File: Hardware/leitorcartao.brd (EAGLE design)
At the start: 34.5 x 56.7 mm, 156 parts, among them IC1 TL084, IC2 TL084, Q1 DMN3404, Q4 BC847ALT1SMD, Q5 BC847ALT1SMD, Q6 BC847ALT1SMD, Q7 BC847ALT1SMD, Q8 MMBT4403, Q9 MMBT4401, U1 SAMD20E14A-AUT, U3 TLV1117-50CDCYR, U4 MFRC52202HN1, U5 LP2985-33DBVR, X1 ANTENA, X2 MIFARE ANTENA

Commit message: Mudanças no layout.
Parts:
- removed X2: MIFARE ANTENA, con-molex:22-23-2021
- added C13, C58: 0.1u, RFiD:C0402
- added X3: ANTENA, RFiD:22-23-2021
- added Y2: (no value), RFiD:HC49/S
- D1: value (none) -> BYG20J; device RFiD:DO214AA -> RFiD:SMA
- D3: value US1J-13-F -> BYG20J
- SWD: device pinhead:1X05 -> RFiD:1X05
- X1: value ANTENA -> MIFARE; device con-molex:22-23-2021 -> RFiD:22-23-2021
- moved R50 176.9 mm to (28.6, 48.1), turned to 90 degrees
- moved C19 142.3 mm to (43.9, 29.1)
- moved C24 142.3 mm to (43.9, 19.5)
- moved C29 142.3 mm to (43.9, 14.7)
- moved R16 142.3 mm to (43.9, 24.3)
- moved R20 142.3 mm to (43.9, 9.90)
- moved R49 142.3 mm to (43.9, 6.50)
- moved Q9 126.8 mm to (12.4, 44.2), flipped to the bottom
- moved Q8 120.0 mm to (12.4, 44.2), turned to 180 degrees
- moved C18 109.0 mm to (30.6, 41.3), flipped to the bottom, turned to 90 degrees
- moved C16 106.8 mm to (31.2, 43.1), flipped to the bottom
- moved Q1 106.7 mm to (12.4, 40.2)
- moved R9 101.7 mm to (32.4, 40.7), flipped to the bottom, turned to 180 degrees
- moved R7 98.8 mm to (32.4, 41.9), flipped to the bottom
- moved R4 96.8 mm to (33.0, 43.7), flipped to the bottom, turned to 270 degrees
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- renumbered QZ1 to Y1
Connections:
- new net XIN: C58.1, U1.15, Y2.1
- new net XOUT: C13.1, U1.16, Y2.2
- net +12V: now also D1.K; no longer D1.C
- net GND: now also C13.2, C58.2
- net N$11: now also X3.1; no longer X1.1
- net N$38: now also X1.1; no longer X2.2
- net N$39: now also X1.2; no longer X2.1
- net N$9: now also X3.2; no longer X1.2
- net USART-RX: no longer U1.15
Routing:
- net USART-RX: track 15.1 -> 0.00 mm
- net +5V: track 37.1 -> 22.4 mm
- net LED-INPUT: track 13.9 -> 1.75 mm
- net MIFARE-SDA: track 15.4 -> 9.24 mm, vias 1 -> 0
- net D0/TX/CLK: track 5.77 -> 0.00 mm
- net MIFARE-SCL: track 10.8 -> 5.27 mm, vias 3 -> 2
- net CARD-PRES: track 5.21 -> 0.00 mm
- net N$41: track 4.71 -> 0.00 mm
- net D1/DATA: track 4.34 -> 0.00 mm
- net +12V: track 80.4 -> 78.4 mm
- net BUZZER: track 2.11 -> 0.11 mm
- net GND: track 39.5 -> 41.3 mm, vias 34 -> 38
- net VCC/2: track 2.22 -> 0.37 mm
- net N$39: track 2.56 -> 0.73 mm
- net N$38: track 2.56 -> 0.73 mm
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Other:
- board text added: "1"
- board text added: "10"
- board text added: "15"
- board text added: "20"
- board text added: "5"

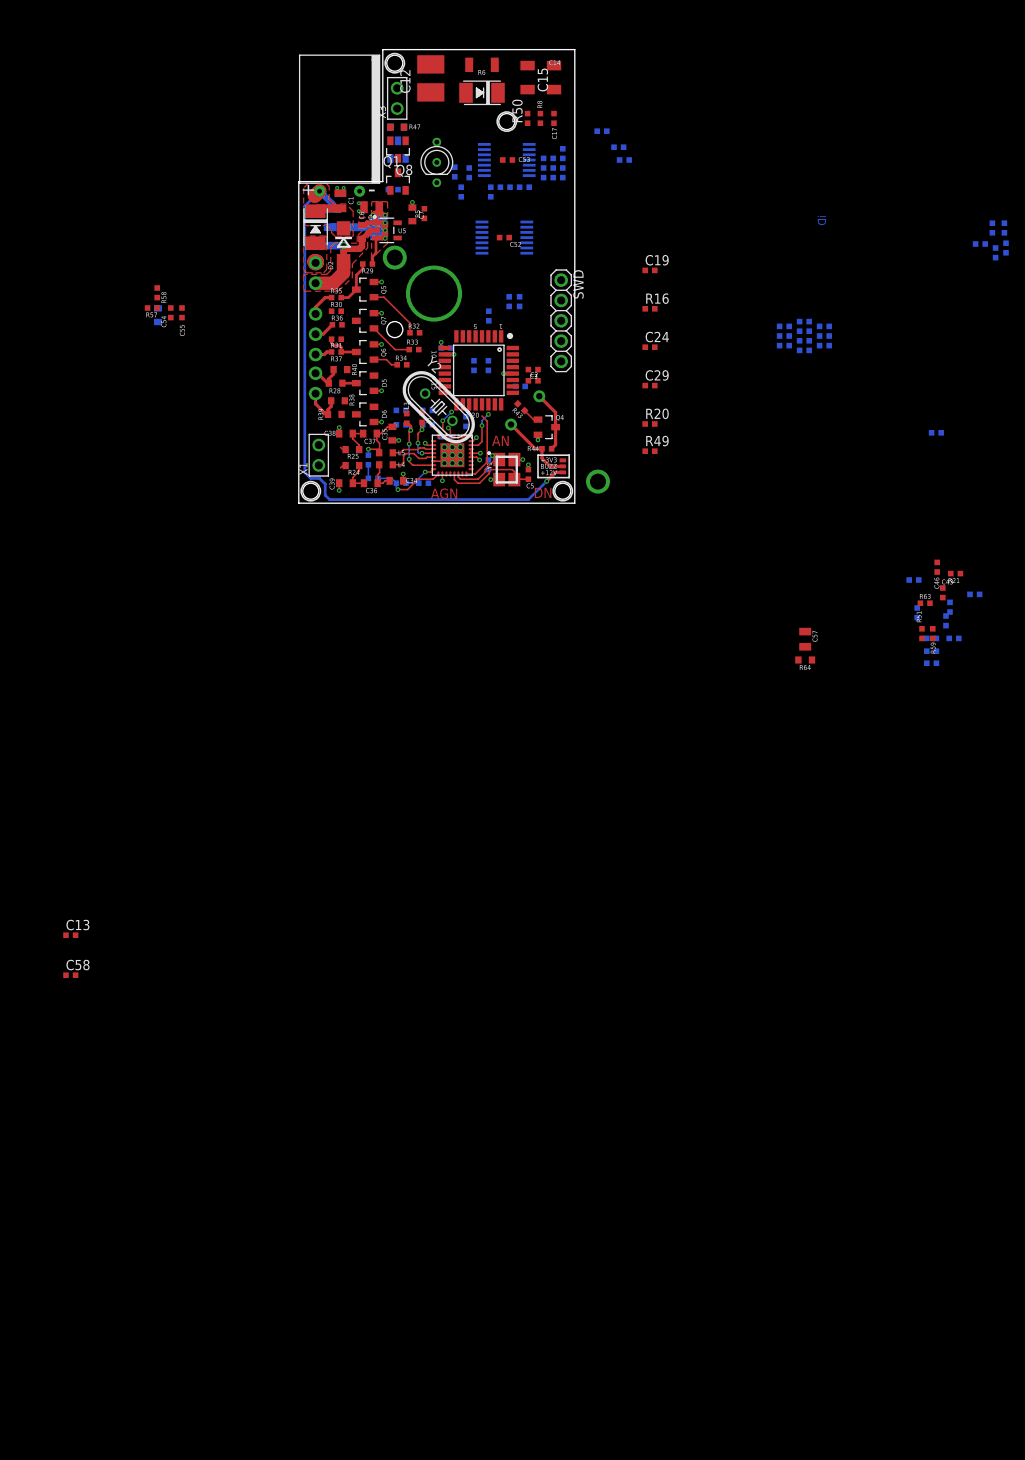
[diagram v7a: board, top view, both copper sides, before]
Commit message: Nova versão do roteamento. Tentativa de isolar tudo no top para DFM.
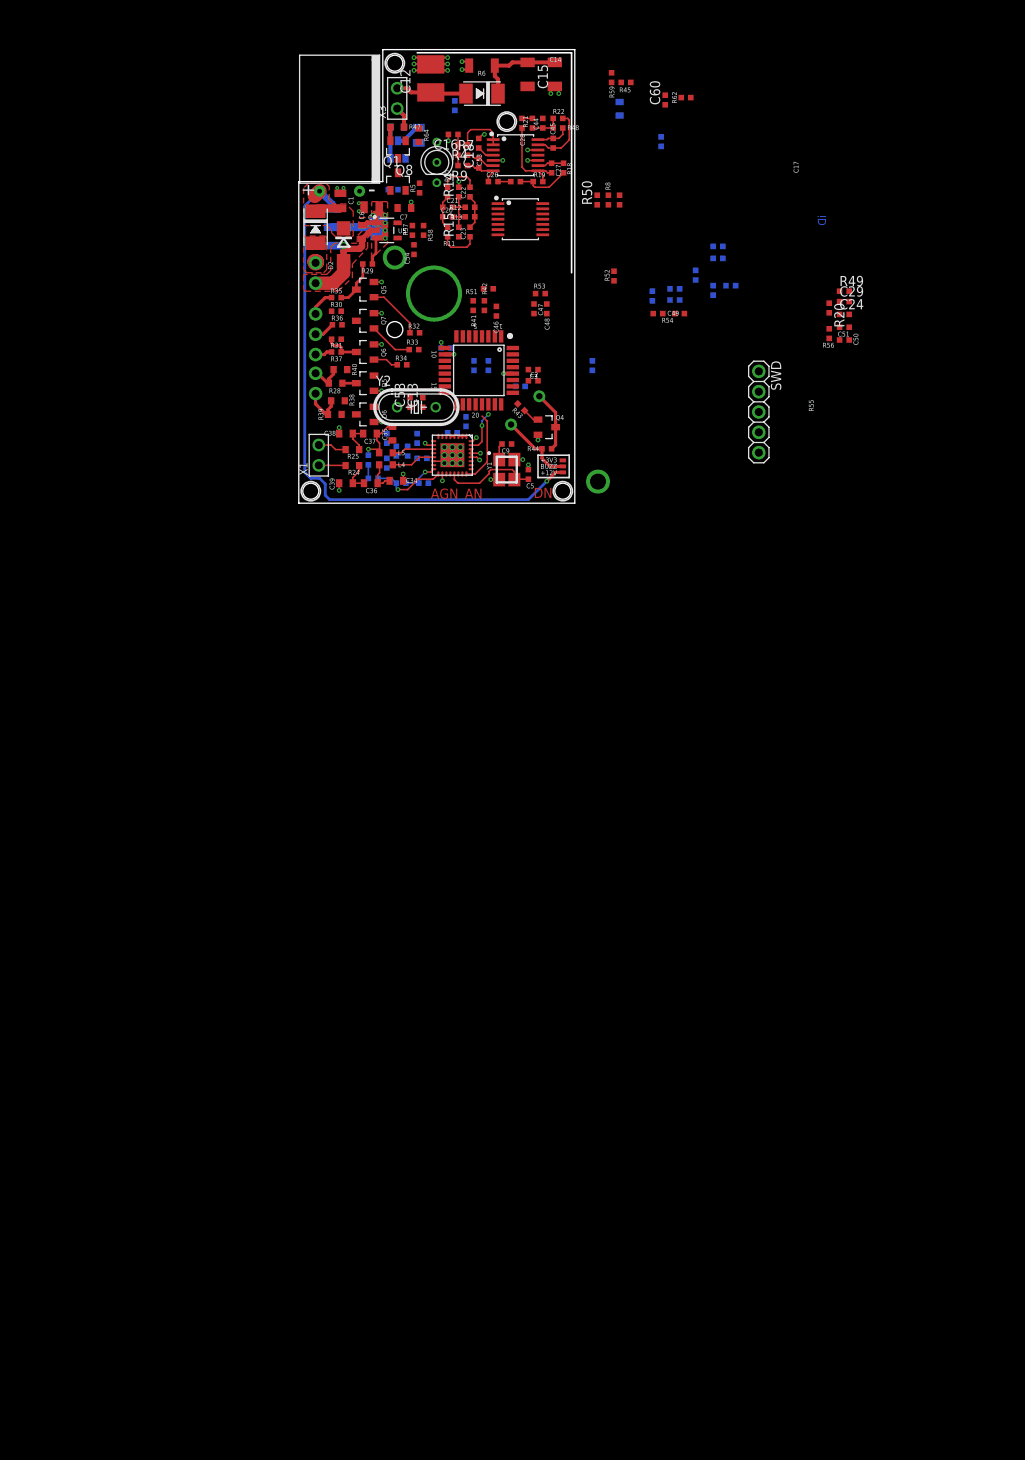
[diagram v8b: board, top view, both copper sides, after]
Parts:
- added C59, C60: 0.1u, RFiD:C0402
- moved C58 83.2 mm to (13.9, 12.6), turned to 90 degrees
- moved R64 81.5 mm to (15.0, 46.0), turned to 270 degrees
- moved R59 80.3 mm to (39.1, 53.2)
- moved C13 79.8 mm to (15.5, 12.6), turned to 90 degrees
- moved C57 79.4 mm to (15.0, 46.0), flipped to the bottom, turned to 270 degrees
- moved R21 77.3 mm to (29.2, 47.5), turned to 270 degrees
- moved C45 77.2 mm to (31.8, 45.0), flipped to the top, turned to 90 degrees
- moved C28 75.2 mm to (27.9, 47.5), flipped to the top, turned to 90 degrees
- moved R51 69.2 mm to (23.7, 26.8), turned to 0 degrees
- moved R53 67.3 mm to (30.2, 26.2), flipped to the top, turned to 0 degrees
- moved R42 65.7 mm to (23.2, 24.7), flipped to the top
- moved R41 65.6 mm to (21.8, 24.7), flipped to the top
- moved C47 64.6 mm to (29.4, 24.3), flipped to the top, turned to 270 degrees
- moved C48 64.4 mm to (31.0, 24.3), flipped to the top, turned to 270 degrees
- moved C46 63.7 mm to (24.7, 24.0)
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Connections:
- net GND: now also C59.2, C60.2
- net V+: now also C59.1, C60.1
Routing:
- net GND: track 41.3 -> 60.0 mm, vias 38 -> 48
- net N$13: track 0.00 -> 11.3 mm
- net N$56: track 0.00 -> 10.5 mm
- net ASK: track 0.00 -> 9.94 mm
- net N$4: track 9.71 -> 0.00 mm, vias 3 -> 0
- net N$9: track 0.00 -> 8.88 mm
- net N$64: track 0.00 -> 7.86 mm
- net N$17: track 0.00 -> 7.00 mm
- net N$22: track 0.00 -> 6.73 mm
- net N$2: track 6.56 -> 0.00 mm, vias 3 -> 0
- net N$10: track 0.00 -> 6.53 mm
- net N$5: track 8.20 -> 2.09 mm, vias 1 -> 0
- net N$11: track 0.00 -> 5.36 mm
- net N$23: track 0.00 -> 4.93 mm
- net V+: track 0.00 -> 4.50 mm, vias 0 -> 4
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- added copper zone on layer 4, net V+
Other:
- outline, holes or cut-outs redrawn
